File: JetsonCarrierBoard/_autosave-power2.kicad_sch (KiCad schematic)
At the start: 18 parts

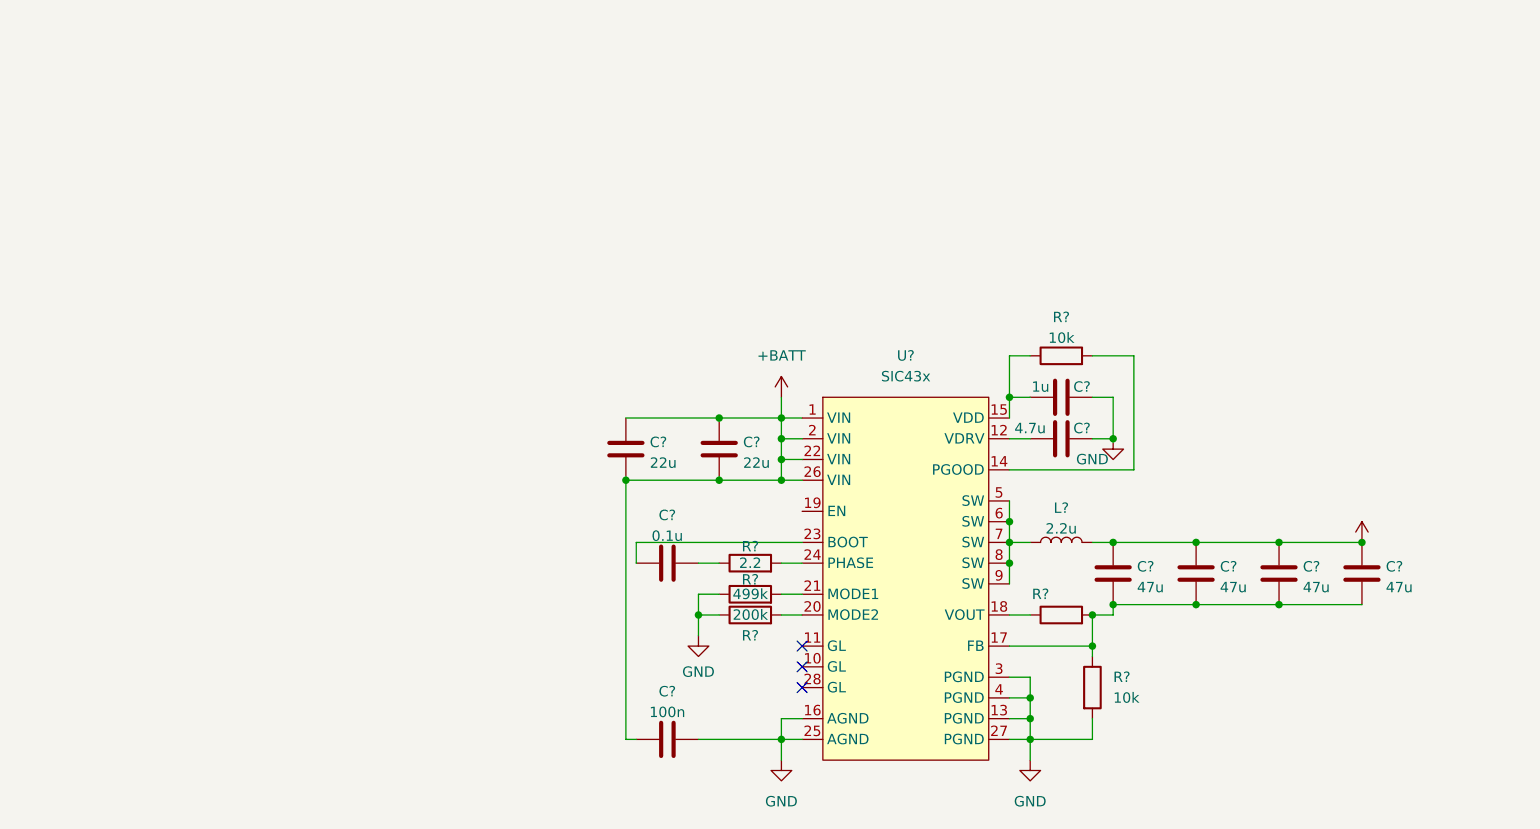
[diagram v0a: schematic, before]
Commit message: Update 3.3V and 1.8V Power + Mic
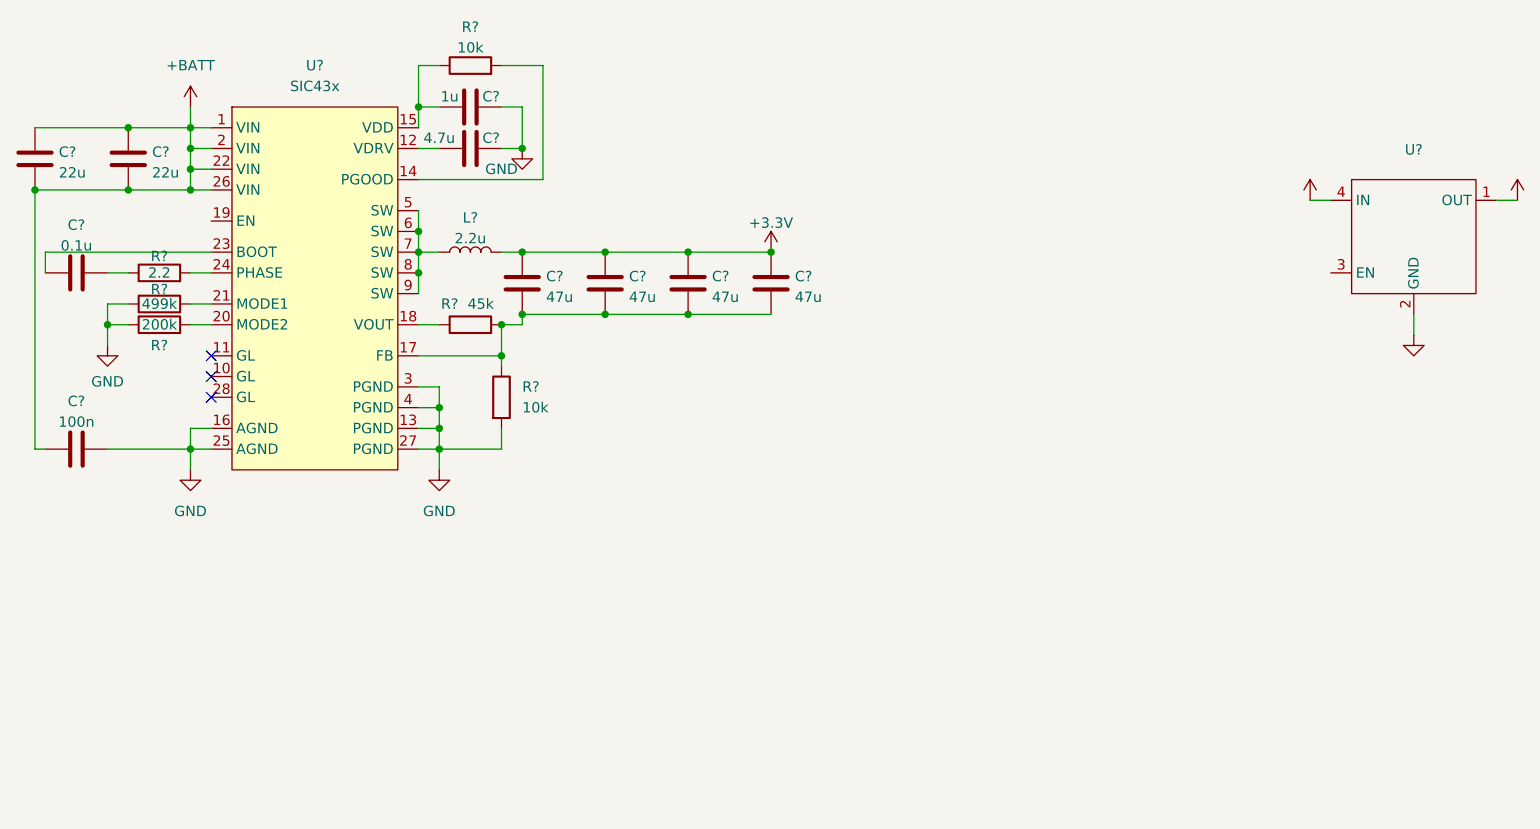
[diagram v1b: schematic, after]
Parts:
- added U?: (no value), symbol Voltage_Regulators_Linear:TLV707
- R?: value (none) -> 45k
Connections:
- net +3V3: now also U?.4 (IN)
- net GND: now also U?.2 (GND)
- new net +1V8: U?.1 (OUT)
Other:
- moved on the sheet: C?, L?, R?, U?
